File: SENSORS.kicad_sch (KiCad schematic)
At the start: 0 parts

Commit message: added micro and 3 sensors and connectors with USB
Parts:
- added C10, C11, C12, C13, C15: 100nF, symbol Device:C
- added R5, R6, R7: 10KΩ 1% 0603, symbol Device:R
- added U4: LSM6DS3, Package_LGA:LGA-14_3x2.5mm_P0.5mm_LayoutBorder3x4y, symbol Sensor_Motion:LSM6DS3
- added U5: H3LIS331DLTR, QFN_31DLTR_STM, symbol MyKiCAD:H3LIS331DLTR
- added U6: MS5611-01BA, Package_LGA:LGA-8_3x5mm_P1.25mm, symbol Sensor_Pressure:MS5611-01BA
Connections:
- new net 3V3: C10.1, C11.1, C12.1, C13.1, C15.1, R5.2, R6.2, R7.2, U4.5 (VDDIO), U4.8 (VDD), U5.1 (VDD_IO), U5.14 (VDD), U5.15 (RESERVED), U6.1 (VDD)
- new net ACC_INT1: U5.9 (INT2)
- new net CS_ACC: R6.1, U5.8 (CS)
- new net CS_BAR: R5.1, U6.4 (CSB), U6.5 (CSB)
- new net CS_IMU: R7.1, U4.12 (CS)
- new net GND: C10.2, C11.2, C12.2, C13.2, C15.2, U4.2 (SDX), U4.3 (SCX), U4.6 (GND), U4.7 (GND), U5.10 (RESERVED), U5.12 (GND), U5.13 (GND), U5.16 (GND), U5.5 (GND), U6.2 (PS), U6.3 (GND)
- new net IMU_INT1: U4.4 (INT1)
- new net SCL: U4.13 (SCL), U5.4 (SCL/SPC), U6.8 (SCLK)
- new net SDA: U4.14 (SDA), U5.6 (SDA/SDI/SDO), U6.7 (SDI/SDA)
- new net SDO: U4.1 (SDO/SA0), U5.7 (SDO/SA0), U6.6 (SDO)
- no-connect marks 0 -> 2
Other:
- note added: "Accelerometer"
- note added: "Barometer"
- note added: "IMU"

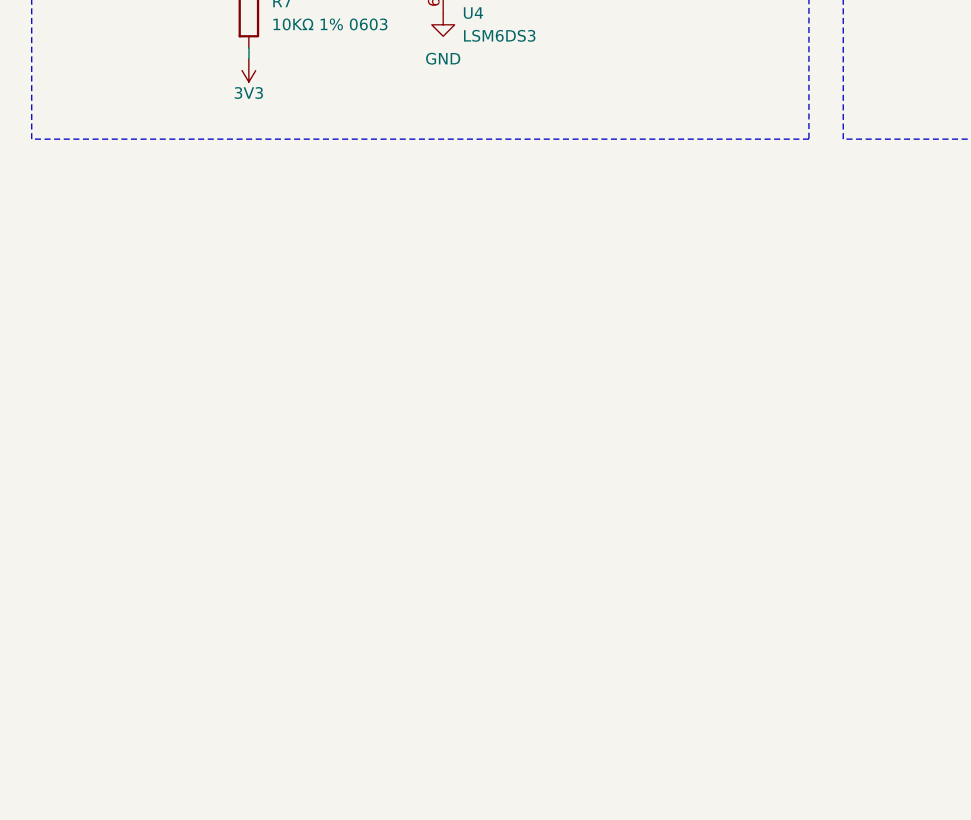
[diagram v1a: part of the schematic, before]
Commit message: added GPS and Temp/Humid sensor
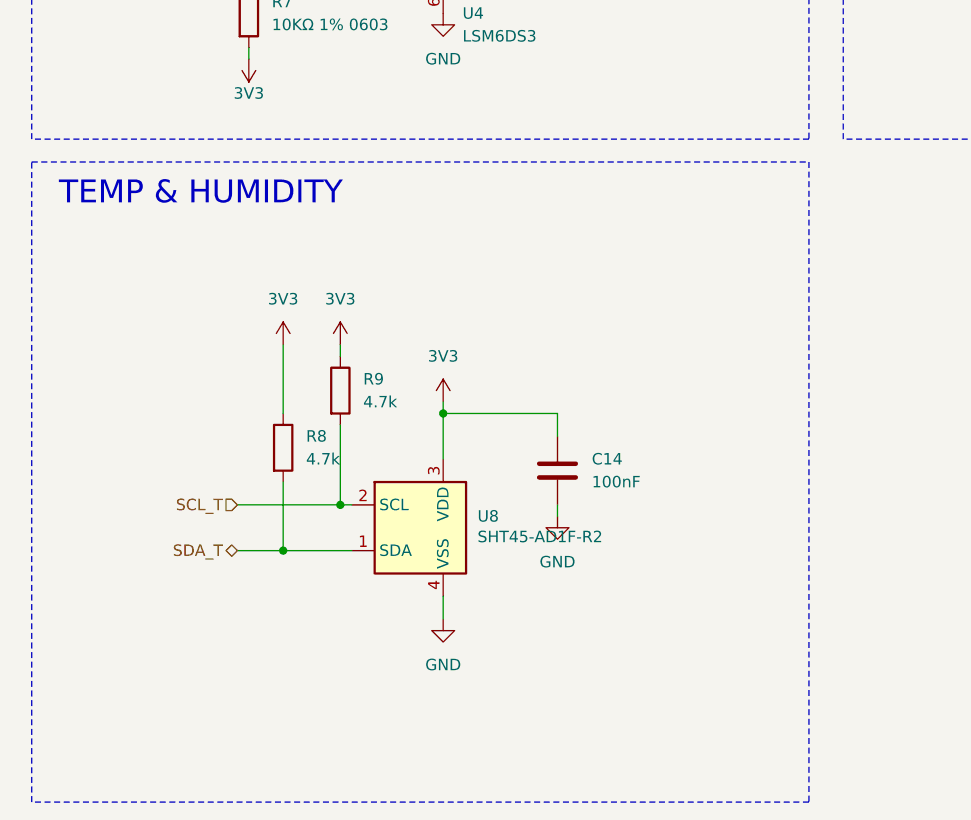
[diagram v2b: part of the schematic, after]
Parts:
- added C14: 100nF, Capacitor_SMD:C_0603_1608Metric, symbol Device:C
- added R8, R9: 4.7k, Resistor_SMD:R_0603_1608Metric, symbol Device:R
- added U8: SHT45-AD1F-R2, Sensor_Humidity:Sensirion_DFN-4_1.5x1.5mm_P0.8mm_SHT4x_NoCentralPad, symbol Sensor_Humidity:SHT4x
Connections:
- net 3V3: now also C14.1, R8.1, R9.1, U8.3 (VDD)
- net GND: now also C14.2, U8.4 (VSS)
- new net SCL_T: R9.2, U8.2 (SCL)
- new net SDA_T: R8.2, U8.1 (SDA)
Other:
- note added: "TEMP & HUMIDITY"

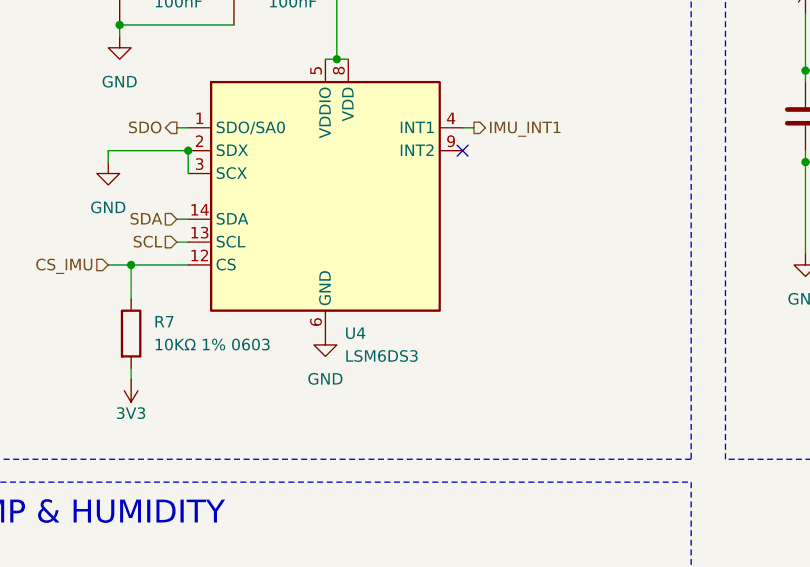
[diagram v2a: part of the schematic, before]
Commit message: added Buzzer, status LEDs
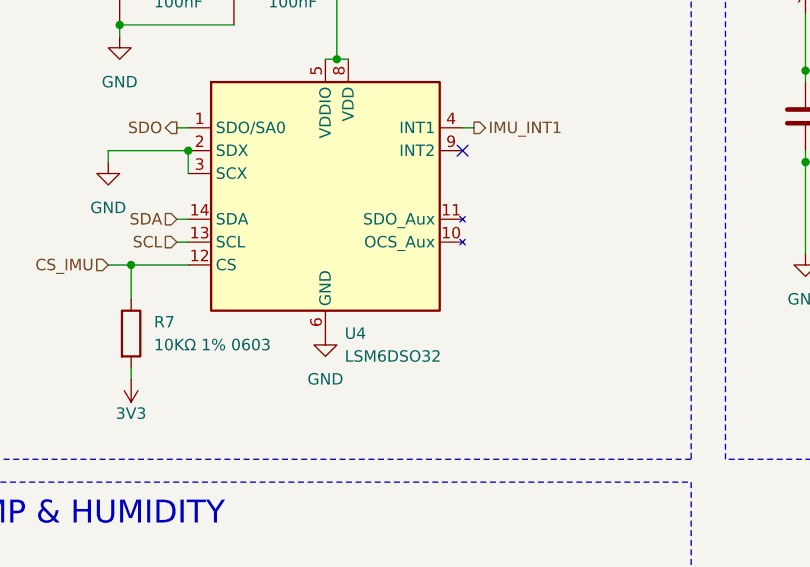
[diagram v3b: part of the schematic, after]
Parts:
- C10, C11, C12, C13, C15: footprint (none) -> Capacitor_SMD:C_0603_1608Metric
- R5, R6, R7: footprint (none) -> Resistor_SMD:R_0603_1608Metric
- U4: value LSM6DS3 -> LSM6DSO32; symbol Sensor_Motion:LSM6DS3 -> MyKiCAD:LSM6DSO32
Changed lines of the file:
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@@
 			)
 		)
-		(property "Footprint" ""
+		(property "Footprint" "Resistor_SMD:R_0603_1608Metric"
 			(at 217.932 62.23 90)
 			(hide yes)
@@
 			)
 		)
-		(property "Footprint" ""
+		(property "Footprint" "Capacitor_SMD:C_0603_1608Metric"
 			(at 182.5752 58.42 0)
 			(hide yes)
@@
 			)
 		)
-		(property "Footprint" ""
+		(property "Footprint" "Capacitor_SMD:C_0603_1608Metric"
 			(at 51.7652 38.1 0)
 			(hide yes)
@@
 			)
 		)
-		(property "Footprint" ""
+		(property "Footprint" "Resistor_SMD:R_0603_1608Metric"
 			(at 134.112 68.58 90)
 			(hide yes)
@@
 	)
 	(symbol
-		(lib_id "Sensor_Motion:LSM6DS3")
+		(lib_id "MyKiCAD:LSM6DSO32")
 		(at 60.96 57.15 0)
 		(unit 1)
@@
 			)
 		)
-		(property "Value" "LSM6DS3"
+		(property "Value" "LSM6DSO32"
 			(at 63.1033 74.93 0)
 			(show_name no)
@@
 			)
 		)
-		(property "Datasheet" "https://www.st.com/resource/en/datasheet/lsm6ds3tr-c.pdf"
+		(property "Datasheet" "https://www.st.com/resource/en/datasheet/lsm6dso32.pdf"
 			(at 63.5 73.66 0)
 			(hide yes)
@@
 			)
 		)
-		(property "Description" "I2C/SPI, iNEMO inertial module: always-on 3D accelerometer and 3D gyroscope"
+		(property "Description" "I2C/SPI, iNEMO inertial module: always-on 3D accelerometer (up to 32g) and 3D gyroscope"
 			(at 60.96 57.15 0)
 			(hide yes)
@@
 			)
 		)
-		(property "Footprint" ""
+		(property "Footprint" "Capacitor_SMD:C_0603_1608Metric"
 			(at 115.2652 52.07 0)
 			(hide yes)
@@
 			)
 		)
-		(property "Footprint" ""
+		(property "Footprint" "Capacitor_SMD:C_0603_1608Metric"
 			(at 216.8652 43.18 0)
 			(hide yes)
@@
 			)
 		)
-		(property "Footprint" ""
+		(property "Footprint" "Capacitor_SMD:C_0603_1608Metric"
 			(at 39.0652 38.1 0)
 			(hide yes)
@@
 			)
 		)
-		(property "Footprint" ""
+		(property "Footprint" "Resistor_SMD:R_0603_1608Metric"
 			(at 37.592 72.39 90)
 			(hide yes)

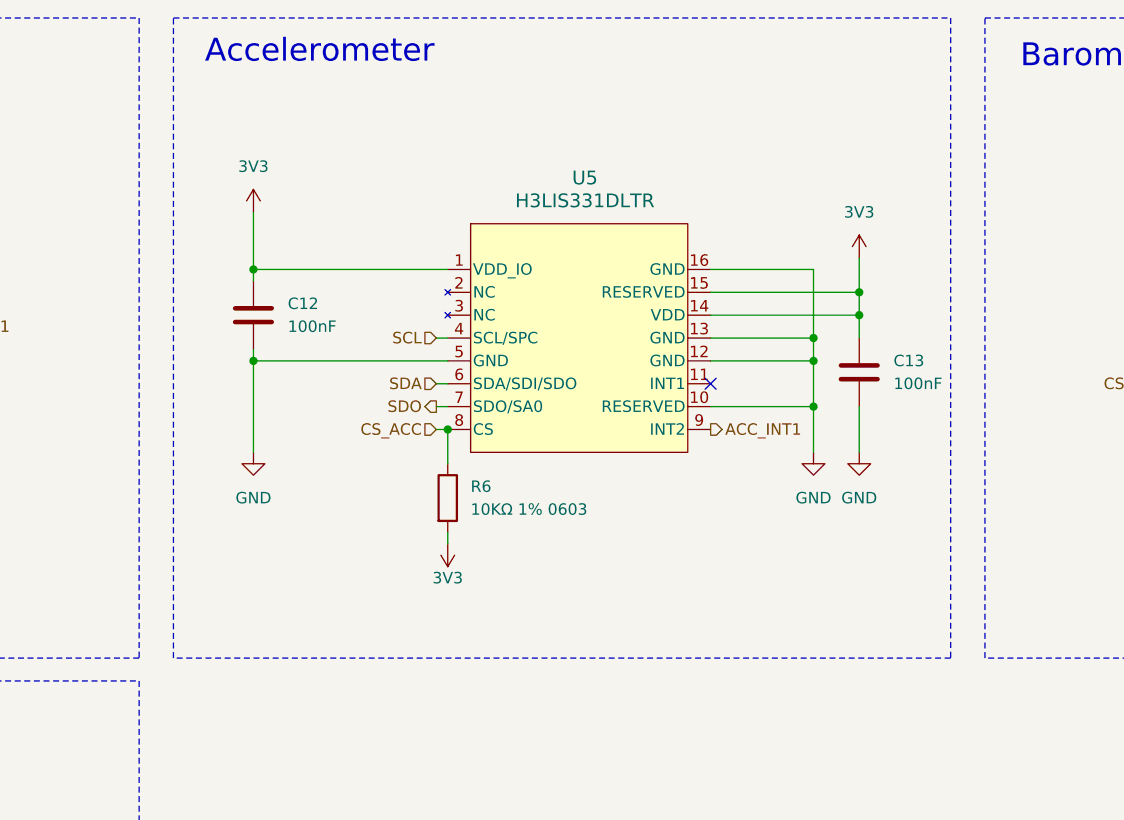
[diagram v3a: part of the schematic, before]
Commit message: Battery protection, camera switch, 64MB flash, ERC clean
- Fuse + TVS on battery input, camera load switch (TPS22917)
- Flash to W25Q512JVFIQ (SOIC-16), hand-solder passive footprints
- Power LED, title blocks, U5 footprint, PWR/NC flags (0 ERC)
- Regenerated schematic PDF
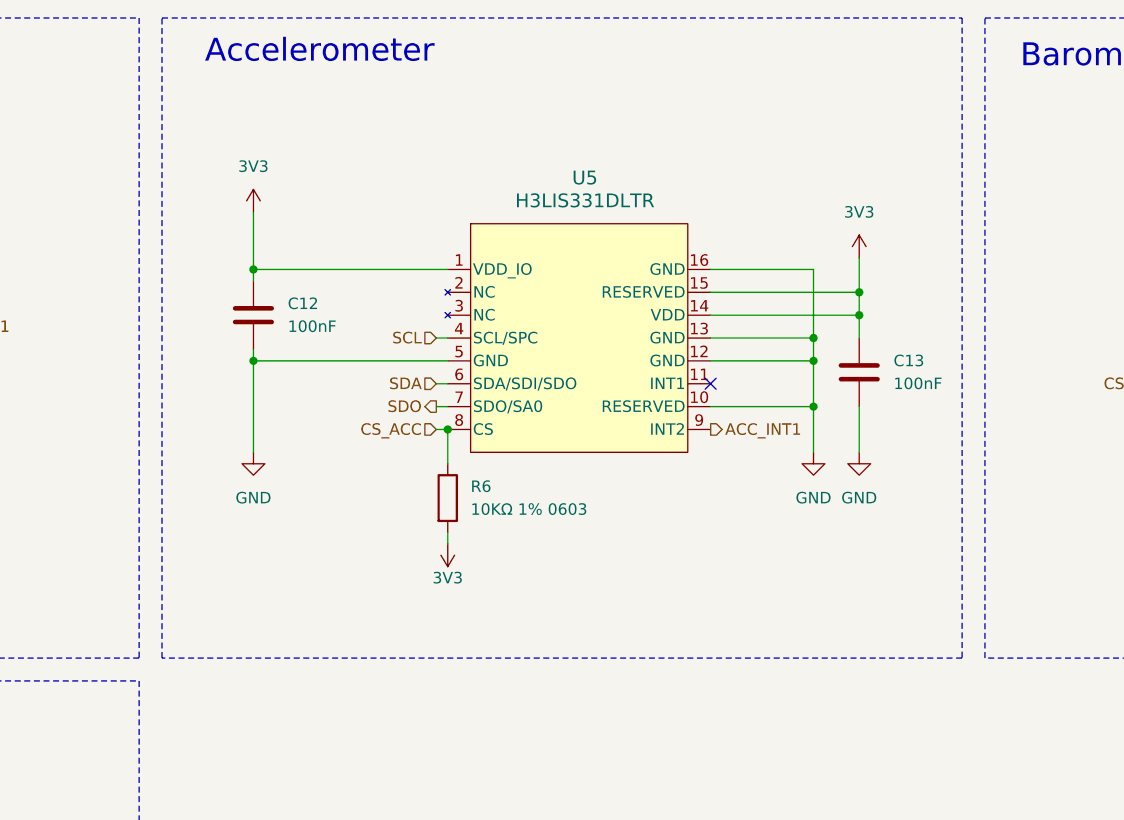
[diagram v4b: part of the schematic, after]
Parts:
- C10, C11, C12, C13, C14, C15: footprint Capacitor_SMD:C_0603_1608Metric -> Capacitor_SMD:C_0603_1608Metric_Pad1.08x0.95mm_HandSolder
- R5, R6, R7, R8, R9: footprint Resistor_SMD:R_0603_1608Metric -> Resistor_SMD:R_0603_1608Metric_Pad0.98x0.95mm_HandSolder
- U5: footprint QFN_31DLTR_STM -> Package_LGA:LGA-16_3x3mm_P0.5mm_LayoutBorder3x5y
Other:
- title: (none) -> Sensors: IMU, High-G, Baro, Temp/Humidity
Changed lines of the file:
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@@
 	(generator_version "10.0")
 	(paper "A4")
+	(title_block
+		(title "Sensors: IMU, High-G, Baro, Temp/Humidity")
+		(date "2026-10-23")
+		(comment 1 "Author: Malek Albdoor")
+	)
 	(rectangle
 		(start 195.58 15.24)
@@
 	)
 	(rectangle
-		(start 105.41 15.24)
-		(end 191.77 86.36)
+		(start 104.14 15.24)
+		(end 193.04 86.36)
 		(stroke
 			(width 0)
@@
 			)
 		)
-		(property "Footprint" "Capacitor_SMD:C_0603_1608Metric"
+		(property "Footprint" "Capacitor_SMD:C_0603_1608Metric_Pad1.08x0.95mm_HandSolder"
 			(at 74.6252 127 0)
 			(hide yes)
@@
 			)
 		)
-		(property "Footprint" "Resistor_SMD:R_0603_1608Metric"
+		(property "Footprint" "Resistor_SMD:R_0603_1608Metric_Pad0.98x0.95mm_HandSolder"
 			(at 47.752 114.3 90)
 			(hide yes)
@@
 			)
 		)
-		(property "Footprint" "Resistor_SMD:R_0603_1608Metric"
+		(property "Footprint" "Resistor_SMD:R_0603_1608Metric_Pad0.98x0.95mm_HandSolder"
 			(at 217.932 62.23 90)
 			(hide yes)
@@
 			)
 		)
-		(property "Footprint" "Capacitor_SMD:C_0603_1608Metric"
+		(property "Footprint" "Capacitor_SMD:C_0603_1608Metric_Pad1.08x0.95mm_HandSolder"
 			(at 182.5752 58.42 0)
 			(hide yes)
@@
 			)
 		)
-		(property "Footprint" "Capacitor_SMD:C_0603_1608Metric"
+		(property "Footprint" "Capacitor_SMD:C_0603_1608Metric_Pad1.08x0.95mm_HandSolder"
 			(at 51.7652 38.1 0)
 			(hide yes)
@@
 			)
 		)
-		(property "Footprint" "Resistor_SMD:R_0603_1608Metric"
+		(property "Footprint" "Resistor_SMD:R_0603_1608Metric_Pad0.98x0.95mm_HandSolder"
 			(at 134.112 68.58 90)
 			(hide yes)
@@
 			)
 		)
-		(property "Footprint" "Capacitor_SMD:C_0603_1608Metric"
+		(property "Footprint" "Capacitor_SMD:C_0603_1608Metric_Pad1.08x0.95mm_HandSolder"
 			(at 115.2652 52.07 0)
 			(hide yes)
@@
 			)
 		)
-		(property "Footprint" "QFN_31DLTR_STM"
+		(property "Footprint" "Package_LGA:LGA-16_3x3mm_P0.5mm_LayoutBorder3x5y"
 			(at 118.11 43.18 0)
 			(hide yes)
@@
 			)
 		)
-		(property "Footprint" "Capacitor_SMD:C_0603_1608Metric"
+		(property "Footprint" "Capacitor_SMD:C_0603_1608Metric_Pad1.08x0.95mm_HandSolder"
 			(at 216.8652 43.18 0)
 			(hide yes)
@@
 			)
 		)
-		(property "Footprint" "Resistor_SMD:R_0603_1608Metric"
+		(property "Footprint" "Resistor_SMD:R_0603_1608Metric_Pad0.98x0.95mm_HandSolder"
 			(at 41.402 120.65 90)
 			(hide yes)
@@
 			)
 		)
-		(property "Footprint" "Capacitor_SMD:C_0603_1608Metric"
+		(property "Footprint" "Capacitor_SMD:C_0603_1608Metric_Pad1.08x0.95mm_HandSolder"
 			(at 39.0652 38.1 0)
 			(hide yes)
@@
 			)
 		)
-		(property "Footprint" "Resistor_SMD:R_0603_1608Metric"
+		(property "Footprint" "Resistor_SMD:R_0603_1608Metric_Pad0.98x0.95mm_HandSolder"
 			(at 37.592 72.39 90)
 			(hide yes)

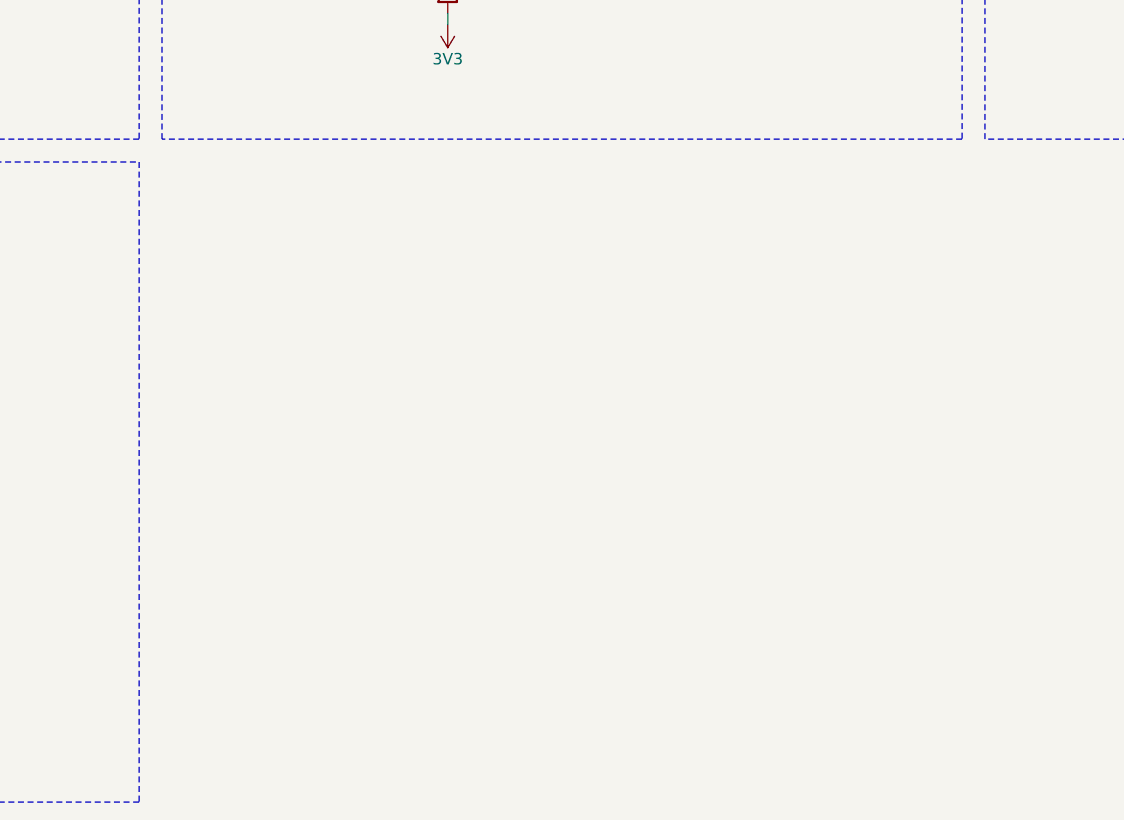
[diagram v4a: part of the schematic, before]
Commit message: updated firmware to fix altitude bug also added mangometer support, updated GUI to have slider for time
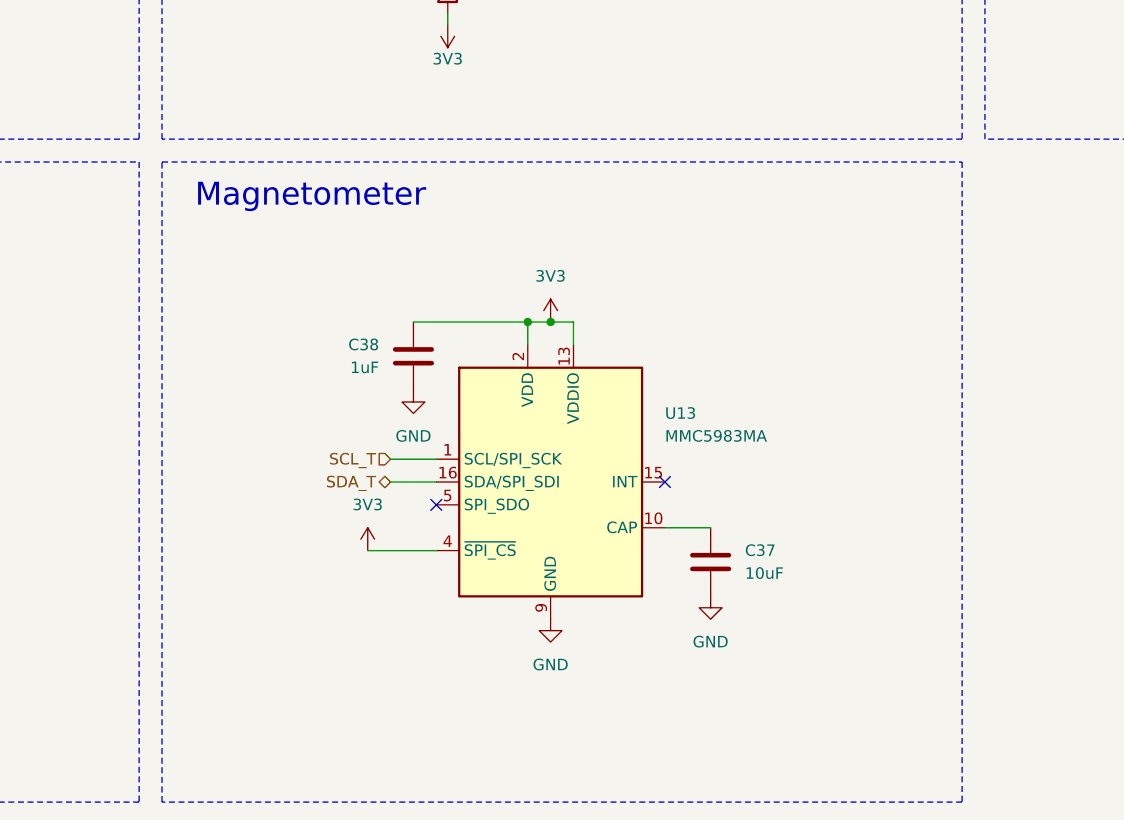
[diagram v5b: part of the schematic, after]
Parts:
- added C37: 10uF, Capacitor_SMD:C_0805_2012Metric_Pad1.18x1.45mm_HandSolder, symbol Device:C
- added C38: 1uF, Capacitor_SMD:C_0603_1608Metric_Pad1.08x0.95mm_HandSolder, symbol Device:C
- added U13: MMC5983MA, Package_LGA:LGA-16_3x3mm_P0.5mm, symbol MyKiCAD:MMC5983MA
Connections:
- net 3V3: now also C38.1, U13.13 (VDDIO), U13.2 (VDD), U13.4 (~{SPI_CS})
- net GND: now also C37.2, C38.2, U13.11 (GND), U13.9 (GND)
- net SCL_T: now also U13.1 (SCL/SPI_SCK)
- net SDA_T: now also U13.16 (SDA/SPI_SDI)
- new net: C37.1, U13.10 (CAP)
- no-connect marks 2 -> 4
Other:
- note added: "Magnetometer"
